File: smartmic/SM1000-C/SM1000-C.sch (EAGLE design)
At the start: 181 parts, among them CN1 HDR100-3, CN10 MJ-3523-SMT, CN11 HDR100-3, CN12 DF11-16DS, CN2 MOLEX-MINI-B-SMT, CN3 RASM722PX, CN4 RJ-45, CN5 MJ-3523-SMT, CN6 SJ-3524-SMT, CN7 MJ-3523-SMT, CN8 SJ-3524-SMT, CN9 MJ-3523-SMT, J1 JMP-2PIN, J3 JMP-2PIN, J4 JMP-2PIN, J5 JMP-2PIN, P1 TPAD50, P10 TPAD50, P11 TPAD50, P12 TPAD50, P13 TPAD50, P14 TPAD50, P15 TPAD50, P16 TPAD50, P17 TPAD50, P18 TPAD50, P19 TPAD50, P2 TPAD50, P20 TPAD50, P21 PAD070-035, P22 PAD070-035, P23 PAD070-035, P24 PAD070-035, P3 TPAD50, P4 TPAD50, P5 TPAD50, P6 TPAD50, P7 TPAD50, P8 TPAD50, P9 TPAD50, SW1 SW-BOURNS-7914S, SW2 SW-BOURNS-7914S, SW3 DPDT, SW4 SW-BOURNS-7914S, T1 SM-LP-5001, T2 SM-LP-5001, U1 STM32F405, U2 LD3985M33R, U3 STMPS2141, U4 EMIF02-USB03F2, U5 TPS54329E, U6 LMV341, U7 LMV341, U8 LM386M-1, U9 LMV341

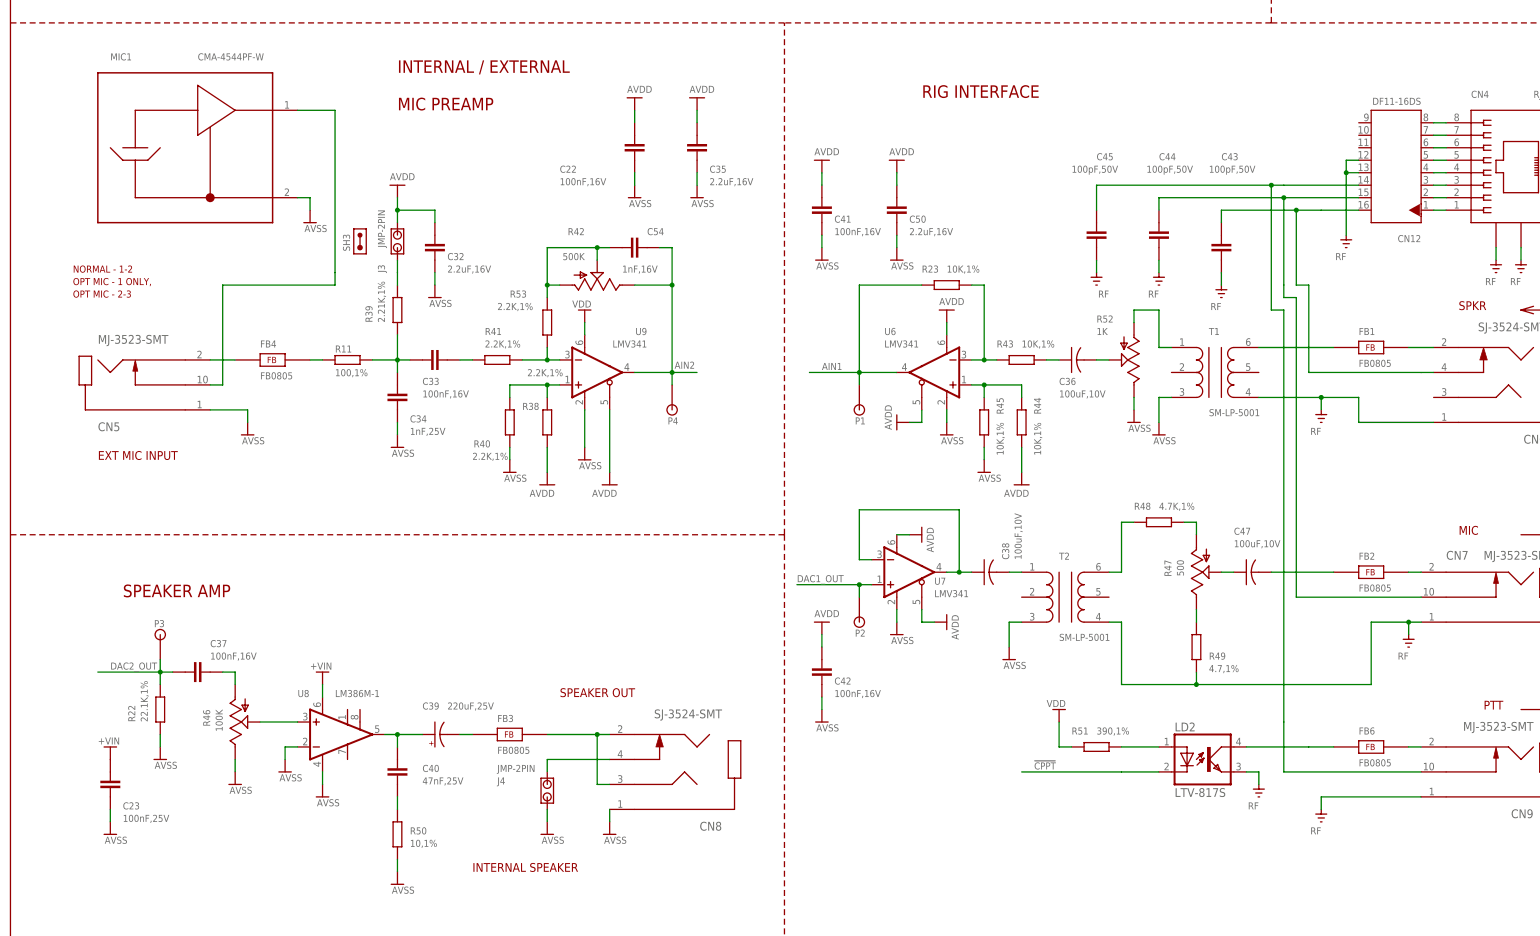
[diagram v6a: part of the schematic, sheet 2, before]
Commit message: Schematic & PCB changes  RGB 09/24/14
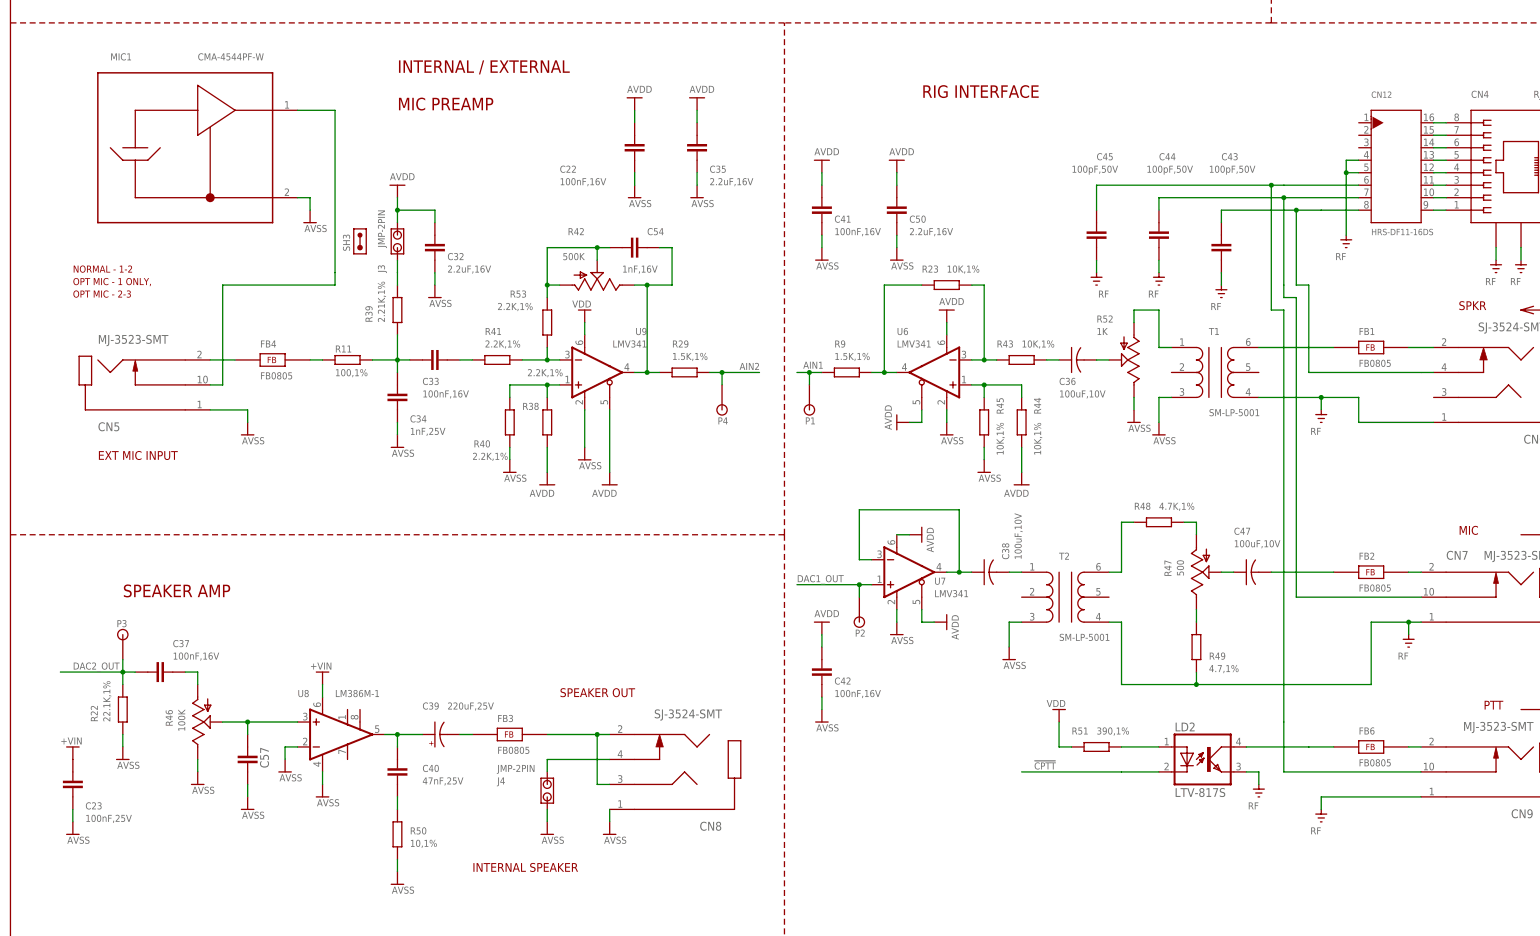
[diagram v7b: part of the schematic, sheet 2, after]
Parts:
- added C55, C56: 1nF,16V, AA-ipc-7351-capacitor:CAPACITOR_0603
- added C57: (no value), AA-ipc-7351-capacitor:CAPACITOR_0603
- added R29, R9: 1.5K,1%, AA-ipc-7351-resistor:RESISTOR_0603
- CN12: value DF11-16DS -> HRS-DF11-16DS
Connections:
- net !CPPT! renamed !CPTT!
- new net N$27: R23.1, R9.2, U6.OUT
- new net N$32: C54.2, R29.1, R42.1, U9.OUT
- net AIN1: now also C56.1, R9.1; no longer R23.1, U6.OUT
- net AIN2: now also C55.1, R29.2; no longer C54.2, R42.1, U9.OUT
- net APTT: now also CN12.6; no longer CN12.14
- net AVSS: now also C55.2, C56.2, C57.2
- net MIC: now also CN12.7; no longer CN12.15
- net N$39: now also C57.1
- net N$51: now also CN12.16; no longer CN12.8
- net N$52: now also CN12.15; no longer CN12.7
- net N$53: now also CN12.14; no longer CN12.6
- net N$54: now also CN12.13; no longer CN12.5
- net N$55: now also CN12.12; no longer CN12.4
- net N$56: now also CN12.11; no longer CN12.3
- net N$57: now also CN12.10; no longer CN12.2
- net N$58: now also CN12.9; no longer CN12.1
- net RF: now also CN12.4, CN12.5; no longer CN12.12, CN12.13
- net SPKR: now also CN12.8; no longer CN12.16
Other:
- note added: "DNL"
- moved on the sheet: C23, C37, CN12, P1, P3, P4, R22, R46

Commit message: Update changes to SM1000-C schematic  RGB 09/26/14
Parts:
- removed J5: JMP-2PIN, _Coherix:JMP-2PIN
- added R54, R55: 0 Ohm, AA-ipc-7351-resistor:RESISTOR_0603
- added SW5: SW-BOURNS-7914J, SM1000:SW-BOURNS-7914J
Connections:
- new net N$29: R55.2, U1A.PA4
- new net N$36: R54.2, U1A.PA5
- net DAC1_OUT: now also R55.1; no longer U1A.PA4
- net DAC2_OUT: now also R54.1; no longer U1A.PA5
- net GND: now also SW5.P$1, SW5.P$2; no longer J5.1
- net NRST: now also SW5.P$3, SW5.P$4; no longer J5.2
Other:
- moved on the sheet: C49, CN1, J1, LED1, LED2, LED3, LED4, R12, R13, R15, R16, R19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
